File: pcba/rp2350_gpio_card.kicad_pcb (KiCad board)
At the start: 2 copper layers, 26 x 30 mm, 41 parts, among them J1 Conn_01x10_Pin, J2 Conn_01x10_Pin, P1 USB_C_Plug_USB2.0, U1 RP2350_60QFN, U2 W25Q128JVS, U4 AP2127K-3.3, Y1 ABM8-272-T3

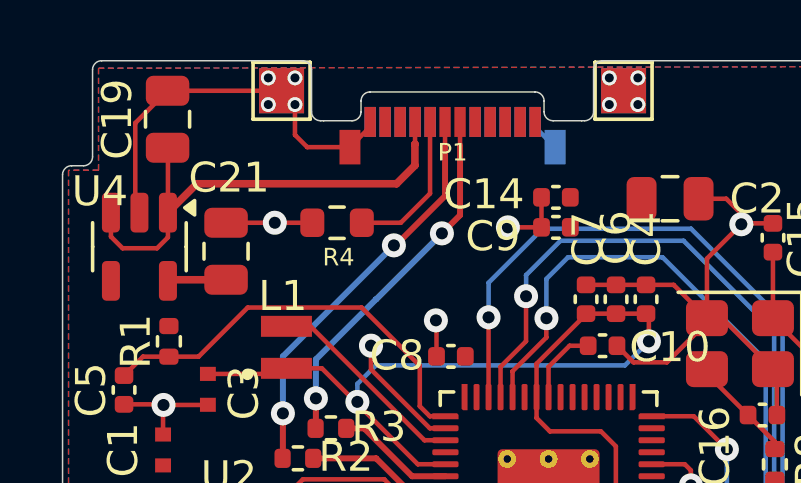
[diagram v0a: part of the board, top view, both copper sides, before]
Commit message: fix usb connection issues
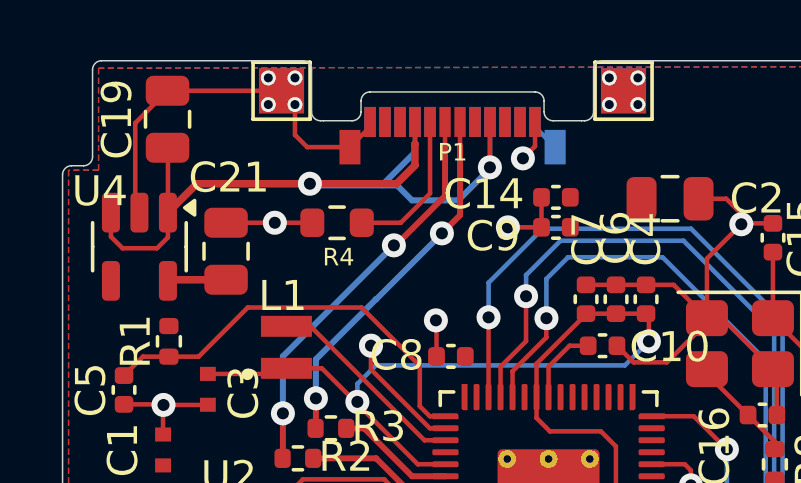
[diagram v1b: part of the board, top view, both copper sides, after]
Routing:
- net VBUS: track 16.3 -> 28.7 mm, vias 0 -> 2
- net GND: track 54.8 -> 56.2 mm, vias 18 -> 19
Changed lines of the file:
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@@
 	)
 	(gr_text "v1.3.2"
-		(at 103.5 59.9 0)
+		(at 103.4 63.1 0)
 		(layer "B.SilkS")
 		(effects
@@
 	)
 	(segment
+		(start 102.300183 55.636434)
+		(end 102.300183 54.926434)
+		(width 0.254)
+		(layer "F.Cu")
+		(net 2)
+	)
+	(segment
+		(start 102.300183 54.926434)
+		(end 102.305183 54.921434)
+		(width 0.254)
+		(layer "F.Cu")
+		(net 2)
+	)
+	(segment
 		(start 101.690183 56.246434)
 		(end 102.300183 55.636434)
@@
 	)
 	(segment
+		(start 104.805183 54.186434)
+		(end 104.805183 55.694817)
+		(width 0.1524)
+		(layer "F.Cu")
+		(net 2)
+	)
+	(segment
 		(start 95.030183 56.246434)
+		(end 94.067683 57.208934)
+		(width 0.254)
+		(layer "F.Cu")
+		(net 2)
+	)
+	(segment
+		(start 94.067683 58.033934)
+		(end 94.067683 57.208934)
+		(width 0.1524)
+		(layer "F.Cu")
+		(net 2)
+	)
+	(segment
+		(start 102.305183 54.186434)
+		(end 102.305183 54.921434)
+		(width 0.1524)
+		(layer "F.Cu")
+		(net 2)
+	)
+	(segment
+		(start 98.8 56.246434)
+		(end 95.030183 56.246434)
+		(width 0.254)
+		(layer "F.Cu")
+		(net 2)
+	)
+	(segment
+		(start 94.067683 55.058934)
+		(end 94.055183 55.046434)
+		(width 0.1524)
+		(layer "F.Cu")
+		(net 2)
+	)
+	(segment
+		(start 104.805183 55.694817)
+		(end 104.8 55.7)
+		(width 0.1524)
+		(layer "F.Cu")
+		(net 2)
+	)
+	(segment
+		(start 93.705183 58.396434)
+		(end 94.067683 58.033934)
+		(width 0.1524)
+		(layer "F.Cu")
+		(net 2)
+	)
+	(segment
+		(start 92.167683 57.208934)
+		(end 92.167683 58.008934)
+		(width 0.1524)
+		(layer "F.Cu")
+		(net 2)
+	)
+	(segment
+		(start 98.8 56.246434)
 		(end 101.690183 56.246434)
 		(width 0.254)
@@
 	)
 	(segment
-		(start 94.067683 57.208934)
-		(end 95.030183 56.246434)
-		(width 0.254)
-		(layer "F.Cu")
-		(net 2)
-	)
-	(segment
-		(start 102.300183 55.636434)
-		(end 102.300183 54.926434)
-		(width 0.254)
-		(layer "F.Cu")
-		(net 2)
-	)
-	(segment
-		(start 94.067683 58.033934)
-		(end 94.067683 57.208934)
-		(width 0.1524)
-		(layer "F.Cu")
-		(net 2)
-	)
-	(segment
-		(start 102.305183 54.186434)
-		(end 102.305183 54.921434)
-		(width 0.1524)
-		(layer "F.Cu")
-		(net 2)
-	)
-	(segment
-		(start 94.067683 55.058934)
-		(end 94.055183 55.046434)
-		(width 0.1524)
-		(layer "F.Cu")
-		(net 2)
-	)
-	(segment
-		(start 102.300183 54.926434)
-		(end 102.305183 54.921434)
-		(width 0.254)
-		(layer "F.Cu")
-		(net 2)
-	)
-	(segment
-		(start 93.705183 58.396434)
-		(end 94.067683 58.033934)
-		(width 0.1524)
-		(layer "F.Cu")
-		(net 2)
-	)
-	(segment
-		(start 92.167683 57.208934)
-		(end 92.167683 58.008934)
-		(width 0.1524)
-		(layer "F.Cu")
-		(net 2)
-	)
-	(segment
 		(start 92.555183 58.396434)
 		(end 93.705183 58.396434)
 		(width 0.1524)
 		(layer "F.Cu")
+		(net 2)
+	)
+	(via
+		(at 104.8 55.7)
+		(size 0.8)
+		(drill 0.4)
+		(layers "F.Cu" "B.Cu")
+		(net 2)
+	)
+	(via
+		(at 98.8 56.246434)
+		(size 0.8)
+		(drill 0.4)
+		(layers "F.Cu" "B.Cu")
+		(net 2)
+	)
+	(segment
+		(start 102.2 56.8)
+		(end 101.7 56.3)
+		(width 0.2)
+		(layer "B.Cu")
+		(net 2)
+	)
+	(segment
+		(start 102.3 55.189634)
+		(end 102.305183 55.194817)
+		(width 0.2)
+		(layer "B.Cu")
+		(net 2)
+	)
+	(segment
+		(start 103.742294 56.8)
+		(end 102.2 56.8)
+		(width 0.2)
+		(layer "B.Cu")
+		(net 2)
+	)
+	(segment
+		(start 104.805183 54.186434)
+		(end 104.805183 55.694817)
+		(width 0.1524)
+		(layer "B.Cu")
+		(net 2)
+	)
+	(segment
+		(start 102.305183 54.186434)
+		(end 102.305183 54.994817)
+		(width 0.1524)
+		(layer "B.Cu")
+		(net 2)
+	)
+	(segment
+		(start 104.8 55.7)
+		(end 104.8 55.742294)
+		(width 0.1524)
+		(layer "B.Cu")
+		(net 2)
+	)
+	(segment
+		(start 104.805183 55.694817)
+		(end 104.8 55.7)
+		(width 0.1524)
+		(layer "B.Cu")
+		(net 2)
+	)
+	(segment
+		(start 98.853566 56.3)
+		(end 98.8 56.246434)
+		(width 0.2)
+		(layer "B.Cu")
+		(net 2)
+	)
+	(segment
+		(start 102.305183 54.994817)
+		(end 102.3 55)
+		(width 0.1524)
+		(layer "B.Cu")
+		(net 2)
+	)
+	(segment
+		(start 101.7 56.3)
+		(end 98.853566 56.3)
+		(width 0.2)
+		(layer "B.Cu")
+		(net 2)
+	)
+	(segment
+		(start 102.305183 55.194817)
+		(end 101.2 56.3)
+		(width 0.2)
+		(layer "B.Cu")
+		(net 2)
+	)
+	(segment
+		(start 102.3 55)
+		(end 102.3 55.189634)
+		(width 0.2)
+		(layer "B.Cu")
+		(net 2)
+	)
+	(segment
+		(start 104.8 55.742294)
+		(end 103.742294 56.8)
+		(width 0.2)
+		(layer "B.Cu")
 		(net 2)
 	)
@@
 	)
 	(segment
+		(start 106.305183 54.994817)
+		(end 105.9 55.4)
+		(width 0.1524)
+		(layer "F.Cu")
+		(net 55)
+	)
+	(segment
 		(start 102.796434 64.396434)
 		(end 103.317683 64.396434)
@@
 	)
 	(segment
+		(start 106.305183 54.186434)
+		(end 106.305183 54.994817)
+		(width 0.1524)
+		(layer "F.Cu")
+		(net 55)
+	)
+	(segment
 		(start 92.605 63.6)
 		(end 93.9 63.6)
@@
 		(size 0.8)
 		(drill 0.4)
+		(layers "F.Cu" "B.Cu")
+		(net 55)
+	)
+	(via
+		(at 105.9 55.4)
+		(size 0.8)
+		(drill 0.4)

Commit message: add OSHW certification
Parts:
- moved REF** 1.41 mm to (112.4, 57.4)

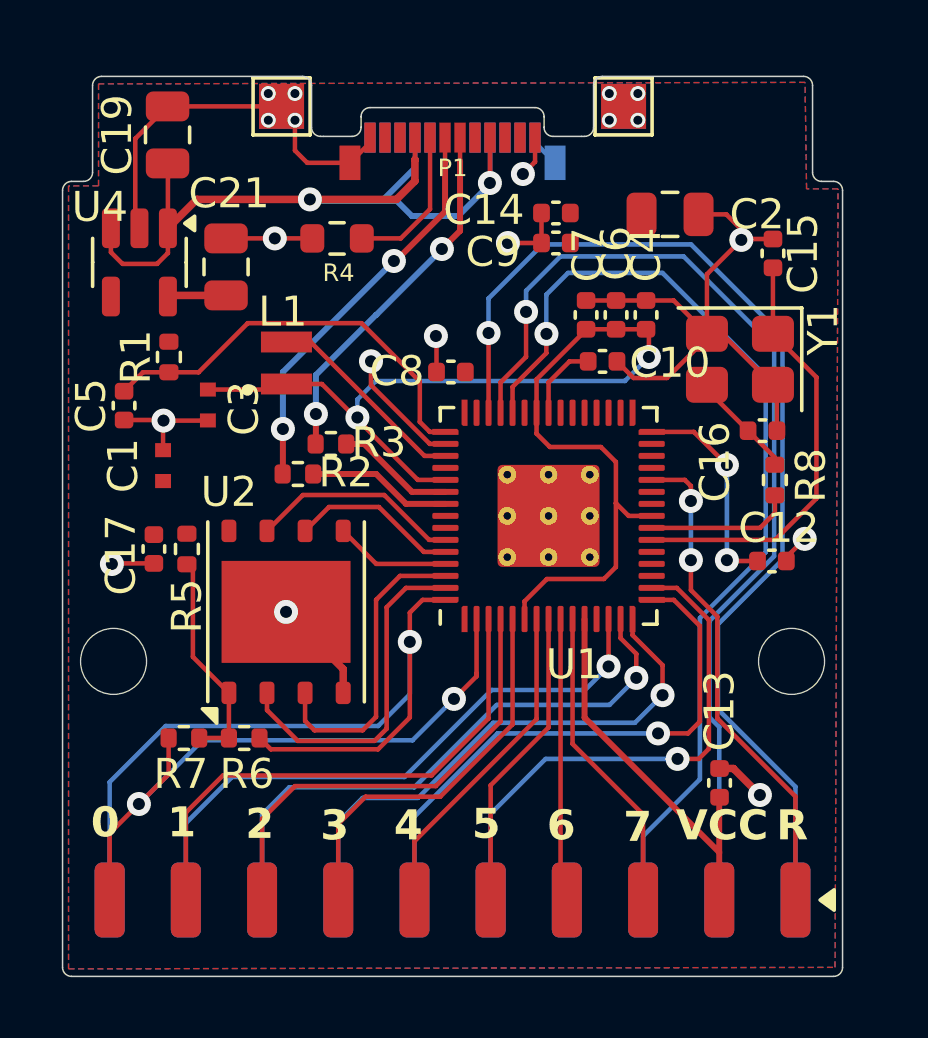
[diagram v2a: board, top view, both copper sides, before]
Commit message: edit silkscreen
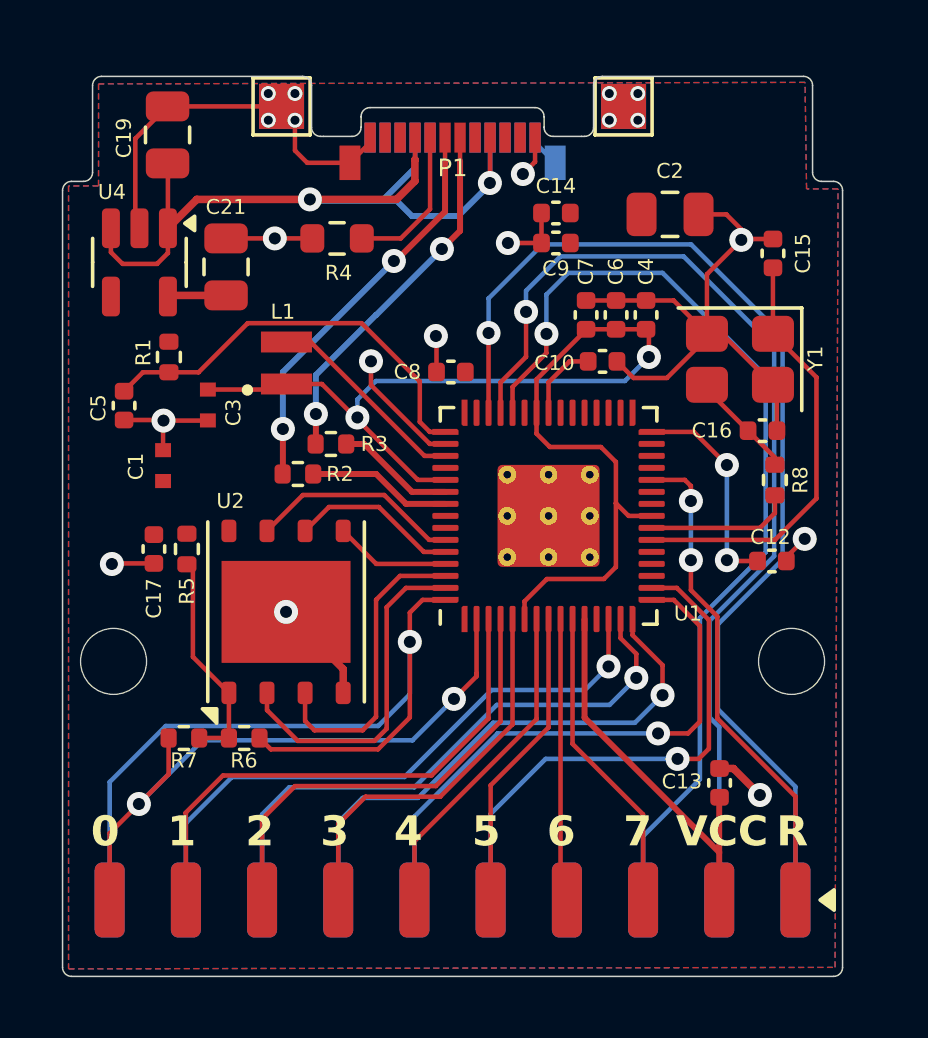
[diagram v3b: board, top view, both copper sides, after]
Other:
- board text added: "C13"

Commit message: edit pcb
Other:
- board text added: "RP2350 GPIO EXPANSION CARD"
- board text removed: "C13"
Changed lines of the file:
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@@
 			(at 0.107836 -0.805183 90)
 			(layer "F.SilkS")
-			(hide yes)
 			(effects
 				(font
@@
 		(layer "Edge.Cuts")
 	)
+	(gr_text "RP2350 GPIO\nEXPANSION CARD"
+		(at 102.5 74.35 0)
+		(layer "F.SilkS")
+		(effects
+			(font
+				(size 1 1)
+				(thickness 0.125)
+			)
+			(justify left bottom)
+		)
+	)
 	(gr_text "3"
 		(at 99.15 77.9 0)
@@
 		)
 	)
-	(gr_text "C13"
-		(at 111.2 75.65 0)
-		(layer "F.SilkS")
-		(effects
-			(font
-				(size 0.5 0.5)
-				(thickness 0.0625)
-			)
-		)
-	)
 	(gr_text "1"
 		(at 94.05 77.9 0)
@@
 		(start 92.167683 58.008934)
 		(end 92.555183 58.396434)
-		(width 0.1524)
+		(width 0.254)
 		(layer "F.Cu")
 		(net 2)
@@
 		(start 94.067683 57.208934)
 		(end 94.067683 55.058934)
-		(width 0.1524)
+		(width 0.254)
 		(layer "F.Cu")
 		(net 2)
@@
 		(start 94.067683 58.033934)
 		(end 94.067683 57.208934)
-		(width 0.1524)
+		(width 0.254)
 		(layer "F.Cu")
 		(net 2)
@@
 		(start 93.705183 58.396434)
 		(end 94.067683 58.033934)
-		(width 0.1524)
+		(width 0.254)
 		(layer "F.Cu")
 		(net 2)
@@
 		(start 92.167683 57.208934)
 		(end 92.167683 58.008934)
-		(width 0.1524)
+		(width 0.254)
 		(layer "F.Cu")
 		(net 2)
@@
 		(start 92.555183 58.396434)
 		(end 93.705183 58.396434)
-		(width 0.1524)
+		(width 0.254)
 		(layer "F.Cu")
 		(net 2)
@@
 		(start 96.005183 57.546434)
 		(end 97.630183 57.546434)
-		(width 0.1524)
+		(width 0.254)
 		(layer "F.Cu")
 		(net 55)
@@
 	)
 	(segment
+		(start 100.805183 54.186434)
+		(end 100.805183 54.356434)
+		(width 0.1524)
+		(layer "F.Cu")
+		(net 55)
+	)
+	(segment
 		(start 110.005183 59.616434)
 		(end 110.925183 59.616434)
@@
 		(start 98.710183 55.026434)
 		(end 98.302183 54.618434)
-		(width 0.1524)
+		(width 0.254)
 		(layer "F.Cu")
 		(net 55)
@@
 	)
 	(segment
-		(start 100.805183 54.186434)
-		(end 100.805183 54.356434)
-		(width 0.1524)
-		(layer "F.Cu")
-		(net 55)
-	)
-	(segment
 		(start 106.52 57.7)
 		(end 106.52 56.7)
@@
 		(start 100.135183 55.026434)
 		(end 98.710183 55.026434)
-		(width 0.1524)
+		(width 0.254)
 		(layer "F.Cu")
 		(net 55)
@@
 		(start 97.855183 53.146434)
 		(end 94.055183 53.146434)
-		(width 0.1524)
+		(width 0.2)
+		(layer "F.Cu")
+		(net 55)
+	)
+	(segment
+		(start 100.135183 55.026434)
+		(end 100.523566 55.026434)
+		(width 0.254)
 		(layer "F.Cu")
 		(net 55)
@@
 	)
 	(segment
-		(start 100.805183 54.356434)
-		(end 100.135183 55.026434)
-		(width 0.1524)
-		(layer "F.Cu")
-		(net 55)
-	)
-	(segment
 		(start 100.835997 62.435997)
 		(end 100.835997 61.643989)
@@
 		(start 97.630183 57.546434)
 		(end 98.880183 57.546434)
-		(width 0.1524)
+		(width 0.254)
+		(layer "F.Cu")
+		(net 55)
+	)
+	(segment
+		(start 100.523566 55.026434)
+		(end 100.787183 54.762817)
+		(width 0.254)
 		(layer "F.Cu")
 		(net 55)
@@
 		(start 98.302183 54.618434)
 		(end 98.302183 53.606934)
-		(width 0.1524)
+		(width 0.254)
 		(layer "F.Cu")
 		(net 55)
@@
 		(layer "F.Cu")
 		(net 55)
+	)
+	(segment
+		(start 100.787183 54.762817)
+		(end 100.787183 54.284878)
+		(width 0.254)
+		(layer "F.Cu")
+		(net 55)

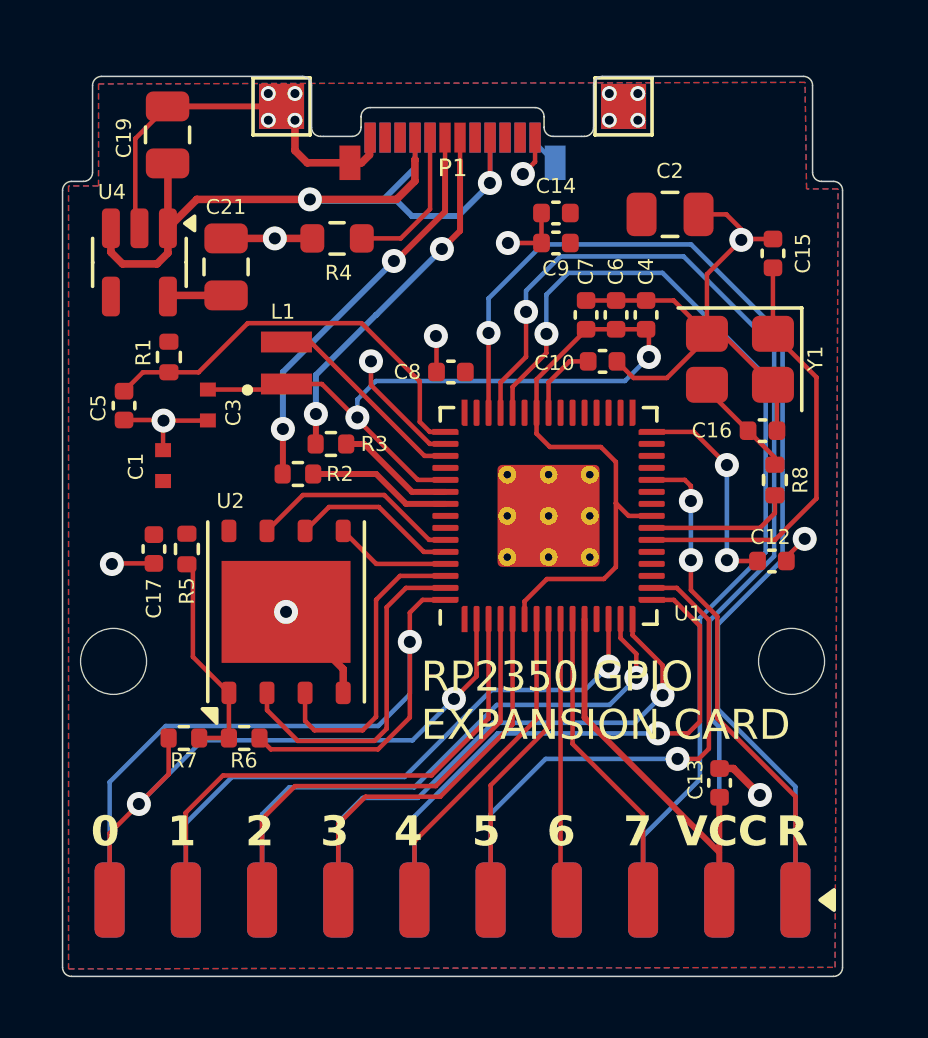
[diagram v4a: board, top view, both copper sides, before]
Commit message: update board, add NextPCB silkscreen, add sponsors to the readme
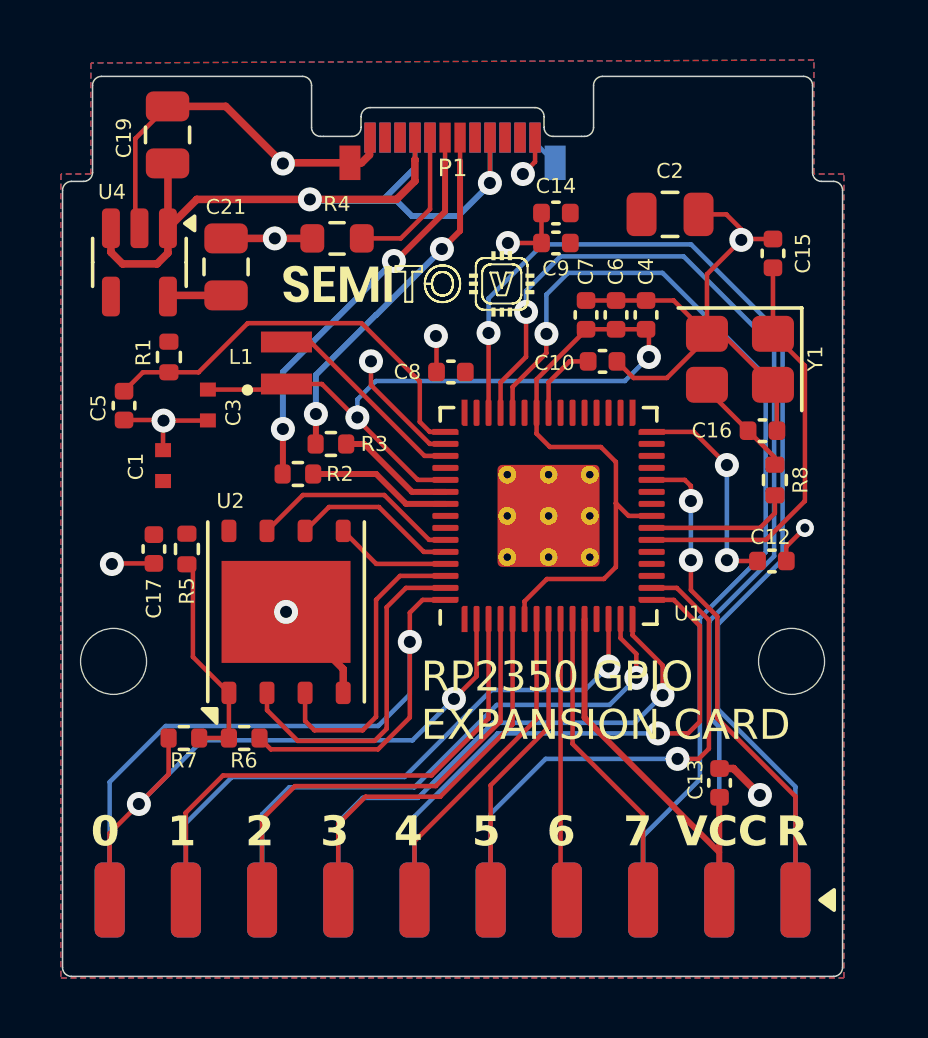
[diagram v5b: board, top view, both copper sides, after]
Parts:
- removed TP1, TP2, TP3, TP4: TestPoint, TestPoint:TestPoint_Pad_1.5x1.5mm
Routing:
- net GND: track 56.5 -> 57.0 mm, vias 19 -> 12
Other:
- copper layers 2 -> 4
- board text added: "Designed by:"
- board text added: "Sponsored by:"
- board text added: "Tan Siret Akıncı, EE student at Polytechnic of Turin"
- board text removed: "Designer: Tan Siret Akıncı"
- board text removed: "EE student at Polytechnic University of Turin"

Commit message: fix inductor magnetism issue and rearrange several other components according to RP2350 datasheet
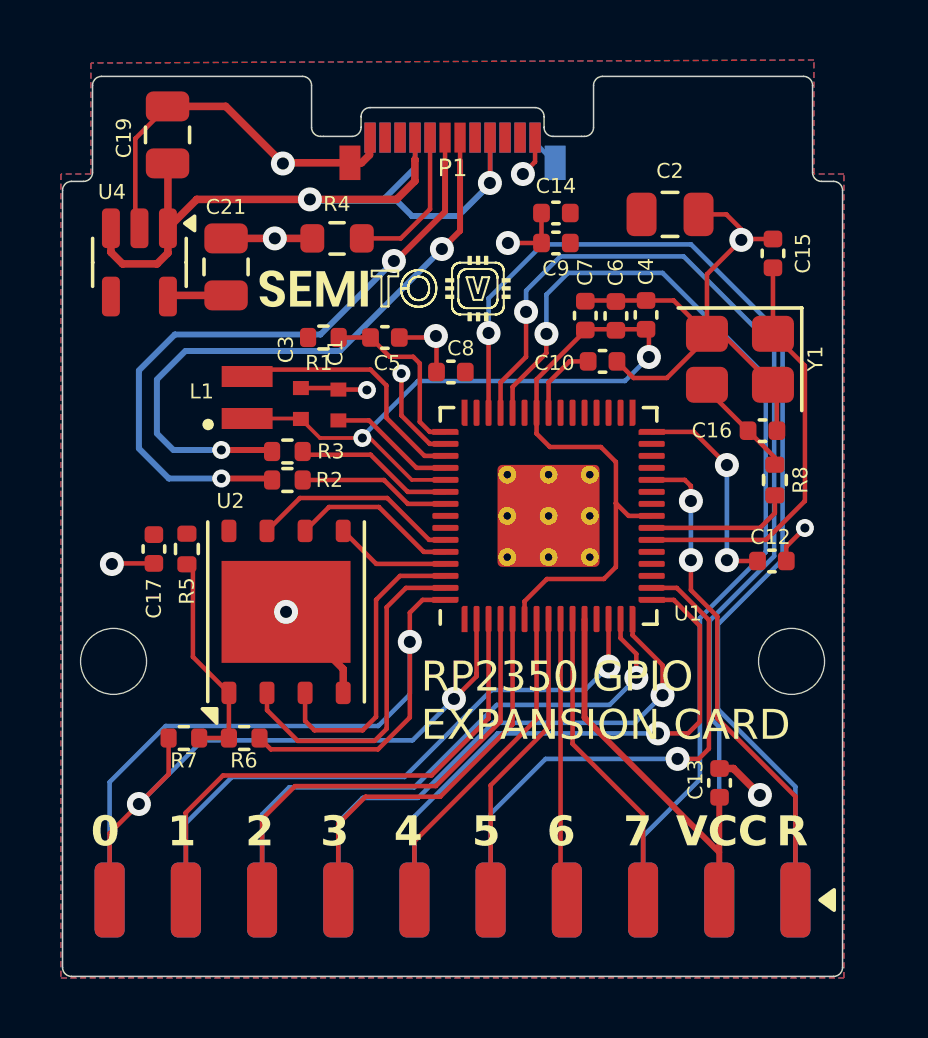
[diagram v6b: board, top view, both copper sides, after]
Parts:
- moved C5 8.99 mm to (101.3, 60.9), turned to 0 degrees
- moved C1 6.18 mm to (99.8, 63.1)
- moved R1 5.19 mm to (99.2, 60.9), turned to 0 degrees
- moved C3 3.10 mm to (98.5, 63.0), turned to 90 degrees
- moved L1 1.74 mm to (96.7, 62.9)
- moved R3 1.47 mm to (98.0, 64.7)
- moved R2 0.40 mm to (98.0, 65.6)
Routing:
- net /USB_D-: track 12.2 -> 21.2 mm
- net /USB_D+: track 13.5 -> 22.3 mm
- net /VREG_AVDD: track 13.9 -> 6.01 mm
- net +3.3V: track 25.4 -> 29.7 mm
- net +1V1: track 39.8 -> 37.5 mm
- net /VREG_LX: track 6.87 -> 8.53 mm
- net Net-(U1-USB_DM): track 3.98 -> 5.50 mm
- net GND: track 57.0 -> 56.0 mm
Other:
- board text added: "v1.3.4"
- board text removed: "v1.3.2"
